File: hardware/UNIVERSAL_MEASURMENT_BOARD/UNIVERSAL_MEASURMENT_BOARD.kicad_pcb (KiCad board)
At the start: 2 copper layers, 9 parts, among them J1 2604-1104, J2 2604-1104, U1 PGA280AIPW, U2 CD4067BM96, U3 CD4067BM96, U4 STM32G0C1KCT6N, U5 ADM3055EBRIZ-RL, U6 ADS8863IDGS, Y2 ECS-1612MV

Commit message: continued
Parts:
- removed the U5 at (148.6, 103.5)
- added C14: 22uF, Capacitor_SMD:C_0805_2012Metric, F.Cu at (137.1, 25.6)
- added C15: 330nF, Capacitor_SMD:C_0805_2012Metric, F.Cu at (137.1, 28.6)
- added C16: 100nF, Capacitor_SMD:C_0805_2012Metric, F.Cu at (137.1, 31.6)
- added C17: 22uF, Capacitor_SMD:C_0805_2012Metric, F.Cu at (137.1, 34.6)
- added C18: 100nF, Capacitor_SMD:C_0603_1608Metric, F.Cu at (154.7, 48.0)
- added C19: 22uF, Capacitor_SMD:C_0805_2012Metric, F.Cu at (137.1, 37.6)
- added C20: 22uF, Capacitor_SMD:C_0805_2012Metric, F.Cu at (137.1, 40.6)
- added C21: 100nF, Capacitor_SMD:C_0603_1608Metric, F.Cu at (154.7, 50.5)
- added C22: 22uF, Capacitor_SMD:C_0805_2012Metric, F.Cu at (137.1, 43.6)
- added C23: 22uF, Capacitor_SMD:C_0805_2012Metric, F.Cu at (137.1, 46.6)
- added C24: 22uF, Capacitor_SMD:C_0805_2012Metric, F.Cu at (137.1, 49.6)
- added C25: 22uF, Capacitor_SMD:C_0805_2012Metric, F.Cu at (141.6, 25.6)
- added C26: 22uF, Capacitor_SMD:C_0805_2012Metric, F.Cu at (141.6, 28.6)
- added C27: 100nF, Capacitor_SMD:C_0805_2012Metric, F.Cu at (141.6, 31.6)
- added C28: 10uF, Capacitor_SMD:C_0805_2012Metric, F.Cu at (141.6, 34.6)
- added C29: 22uF, Capacitor_SMD:C_0805_2012Metric, F.Cu at (141.6, 37.6)
- added C30: 100nF, Capacitor_SMD:C_0603_1608Metric, F.Cu at (154.7, 53.0)
- added C31: 22uF, Capacitor_SMD:C_0805_2012Metric, F.Cu at (141.6, 40.6)
- added C32: 22uF, Capacitor_SMD:C_0805_2012Metric, F.Cu at (141.6, 43.6)
- added C33: 100nF, Capacitor_SMD:C_0603_1608Metric, F.Cu at (154.7, 55.5)
- added C34: 22uF, Capacitor_SMD:C_0805_2012Metric, F.Cu at (141.6, 46.6)
- added C35: 100nF, Capacitor_SMD:C_0805_2012Metric, F.Cu at (141.6, 49.6)
- added C36: 10uF, Capacitor_SMD:C_0805_2012Metric, F.Cu at (146.0, 25.6)
- added C37: 22uF, Capacitor_SMD:C_0805_2012Metric, F.Cu at (146.0, 28.6)
- added C38: 22uF, Capacitor_SMD:C_0805_2012Metric, F.Cu at (146.0, 31.6)
- added C39: 22uF, Capacitor_SMD:C_0805_2012Metric, F.Cu at (146.0, 34.6)
- added C40: 22uF, Capacitor_SMD:C_0805_2012Metric, F.Cu at (146.0, 37.6)
- added C41: 22uF, Capacitor_SMD:C_0805_2012Metric, F.Cu at (146.0, 40.6)
- added C42: 22uF, Capacitor_SMD:C_0805_2012Metric, F.Cu at (146.0, 43.6)
- added C43: 330nF, Capacitor_SMD:C_0805_2012Metric, F.Cu at (146.0, 46.6)
- added C44: 100nF, Capacitor_SMD:C_0805_2012Metric, F.Cu at (146.0, 49.6)
- added C45: 22uF, Capacitor_SMD:C_0805_2012Metric, F.Cu at (150.5, 25.6)
- added C46: 100nF, Capacitor_SMD:C_0603_1608Metric, F.Cu at (154.7, 58.0)
- added C47: 22uF, Capacitor_SMD:C_0805_2012Metric, F.Cu at (150.5, 28.6)
- added C48: 22uF, Capacitor_SMD:C_0805_2012Metric, F.Cu at (150.5, 31.6)
- added C49: 100nF, Capacitor_SMD:C_0603_1608Metric, F.Cu at (154.7, 60.5)
- added C50: 22uF, Capacitor_SMD:C_0805_2012Metric, F.Cu at (150.5, 34.6)
- added C51: 22uF, Capacitor_SMD:C_0805_2012Metric, F.Cu at (150.5, 37.6)
- added C52: 22uF, Capacitor_SMD:C_0805_2012Metric, F.Cu at (150.5, 40.6)
- added C53: 100nF, Capacitor_SMD:C_0805_2012Metric, F.Cu at (150.5, 43.6)
- added C55: 100nF, Capacitor_SMD:C_0805_2012Metric, F.Cu at (150.5, 46.6)
- added C57: -F, Capacitor_SMD:C_0805_2012Metric, F.Cu at (150.5, 49.6)
- added J10: 2604-1104, 2604-1104:26041104, F.Cu at (58.2, 74.8)
- added J11: 2604-1104, 2604-1104:26041104, F.Cu at (58.2, 97.6)
- added J12: 2604-1104, 2604-1104:26041104, F.Cu at (58.2, 120.5)
- added J13: 2604-1104, 2604-1104:26041104, F.Cu at (58.2, 143.3)
- added J14: 2604-1104, 2604-1104:26041104, F.Cu at (58.2, 166.2)
- added J15: 2604-1104, 2604-1104:26041104, F.Cu at (83.7, 29.1)
- added J16: PRG, Connector_PinHeader_1.00mm:PinHeader_1x05_P1.00mm_Vertical, F.Cu at (131.2, 25.6)
- added J17: 2604-1104, 2604-1104:26041104, F.Cu at (83.7, 51.9)
- added J18: 2604-1104, 2604-1104:26041104, F.Cu at (83.7, 74.8)
- added J19: 2604-1104, 2604-1104:26041104, F.Cu at (83.7, 97.6)
- added J20: 2604-1104, 2604-1104:26041104, F.Cu at (83.7, 120.5)
- added J21: 2604-1104, 2604-1104:26041104, F.Cu at (83.7, 143.3)
- added J22: 2604-1104, 2604-1104:26041104, F.Cu at (83.7, 166.2)
- added J23: 2604-1104, 2604-1104:26041104, F.Cu at (109.2, 29.1)
- added J24: 2604-1104, 2604-1104:26041104, F.Cu at (109.2, 51.9)
- added J25: 2604-1104, 2604-1104:26041104, F.Cu at (109.2, 74.8)
- added J26: 2604-1104, 2604-1104:26041104, F.Cu at (109.2, 97.6)
- added J27: 2604-1104, 2604-1104:26041104, F.Cu at (109.2, 120.5)
- added J3: 2604-1104, 2604-1104:26041104, F.Cu at (32.7, 74.8)
- added J4: 2604-1104, 2604-1104:26041104, F.Cu at (32.7, 97.6)
- added J5: 2604-1104, 2604-1104:26041104, F.Cu at (32.7, 120.5)
- added J6: 2604-1104, 2604-1104:26041104, F.Cu at (32.7, 143.3)
- added J7: 2604-1104, 2604-1104:26041104, F.Cu at (32.7, 166.2)
- added J8: 2604-1104, 2604-1104:26041104, F.Cu at (58.2, 29.1)
- added J9: 2604-1104, 2604-1104:26041104, F.Cu at (58.2, 51.9)
- added L1: 68uH/1.4A, Inductor_SMD:L_TDK_VLS6045EX_VLS6045AF, F.Cu at (156.5, 27.8)
- added L2: 68uH/1.4A, Inductor_SMD:L_TDK_VLS6045EX_VLS6045AF, F.Cu at (156.5, 35.4)
- added L3: 68uH/1.4A, Inductor_SMD:L_TDK_VLS6045EX_VLS6045AF, F.Cu at (156.5, 42.9)
- added U10: TPS54202HDDCR, TPS54202HDDCR:SOT95P280X110-6N, F.Cu at (159.3, 53.6)
- added U12: TPS54202HDDCR, TPS54202HDDCR:SOT95P280X110-6N, F.Cu at (159.3, 58.2)
- added U13: ICL7662EBA+, ICL7662EBA+:SOIC127P600X175-8N, F.Cu at (139.1, 54.4)
- added U14: ADM3055EBRIZ-RL, ADM3055EBRIZ-RL:SOIC127P1030X264-20N, F.Cu at (141.3, 72.3)
- added U7: TPS54202HDDCR, TPS54202HDDCR:SOT95P280X110-6N, F.Cu at (159.3, 49.0)
- added U8: AMS1117-3.3, Package_TO_SOT_SMD:SOT-223-3_TabPin2, F.Cu at (165.3, 28.2)
- added U9: AMS1117-3.3, Package_TO_SOT_SMD:SOT-223-3_TabPin2, F.Cu at (165.3, 36.6)
- moved J1 155.8 mm to (32.7, 29.1)
- moved J2 155.8 mm to (32.7, 51.9)
- moved U1 30.5 mm to (188.8, 120.6)
- moved U2 30.5 mm to (190.8, 112.5)
- moved U3 30.5 mm to (148.9, 115.3)
- moved U4 30.5 mm to (146.8, 128.7)
- moved U5 30.5 mm to (161.8, 115.3)
- moved Y1 30.5 mm to (194.8, 120.5)
- renumbered U6 to U1, U4 to U2, U2 to U3, U1 to U4, U3 to U5, Y2 to Y1
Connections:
- net +15V renamed +15VA
- net +3.3V renamed +3.3VA
- net -15V renamed -15VA
- J1 pad 5: Net-(J1-3.1) -> /connectors/A1P
- J1 pad 6: Net-(J1-3.1) -> /connectors/A1P
- J1 pad 7: Net-(J1-4.1) -> /connectors/A1N
- J1 pad 8: Net-(J1-4.1) -> /connectors/A1N
- J2 pad 1: Net-(J2-1.1) -> /connectors/A6N
- J2 pad 2: Net-(J2-1.1) -> /connectors/A6N
- J2 pad 3: Net-(J2-2.1) -> GND
- J2 pad 4: Net-(J2-2.1) -> GND
- U1 pad 2: +3V3 -> +3V3A
- U3 pad 16: /mux & pga/A16P -> /connectors/A16P
- U3 pad 17: /mux & pga/A15P -> /connectors/A15P
- U3 pad 18: /mux & pga/A14P -> /connectors/A14P
- U3 pad 19: /mux & pga/A13P -> /connectors/A13P
- U3 pad 2: /mux & pga/A8P -> /connectors/A8P
- U3 pad 20: /mux & pga/A12P -> /connectors/A12P
- U3 pad 21: /mux & pga/A11P -> /connectors/A11P
- U3 pad 22: /mux & pga/A10P -> /connectors/A10P
- U3 pad 23: /mux & pga/A9P -> /connectors/A9P
- U3 pad 3: /mux & pga/A7P -> /connectors/A7P
- U3 pad 4: /mux & pga/A6P -> /connectors/A6P
- U3 pad 5: /mux & pga/A5P -> /connectors/A5P
- U3 pad 6: /mux & pga/A4P -> /connectors/A4P
- U3 pad 7: /mux & pga/A3P -> /connectors/A3P
- U3 pad 8: /mux & pga/A2P -> /connectors/A2P
- U3 pad 9: /mux & pga/A1P -> /connectors/A1P
- U5 pad 16: /mux & pga/A16N -> /connectors/A16N
- U5 pad 17: /mux & pga/A15N -> /connectors/A15N
- U5 pad 18: /mux & pga/A14N -> /connectors/A14N
- U5 pad 19: /mux & pga/A13N -> /connectors/A13N
- U5 pad 2: /mux & pga/A8N -> /connectors/A8N
- U5 pad 20: /mux & pga/A12N -> /connectors/A12N
- U5 pad 21: /mux & pga/A11N -> /connectors/A11N
- U5 pad 22: /mux & pga/A10N -> /connectors/A10N
- U5 pad 23: /mux & pga/A9N -> /connectors/A9N
- U5 pad 3: /mux & pga/A7N -> /connectors/A7N
- U5 pad 4: /mux & pga/A6N -> /connectors/A6N
- U5 pad 5: /mux & pga/A5N -> /connectors/A5N
- U5 pad 6: /mux & pga/A4N -> /connectors/A4N
- U5 pad 7: /mux & pga/A3N -> /connectors/A3N
- U5 pad 8: /mux & pga/A2N -> /connectors/A2N
- U5 pad 9: /mux & pga/A1N -> /connectors/A1N

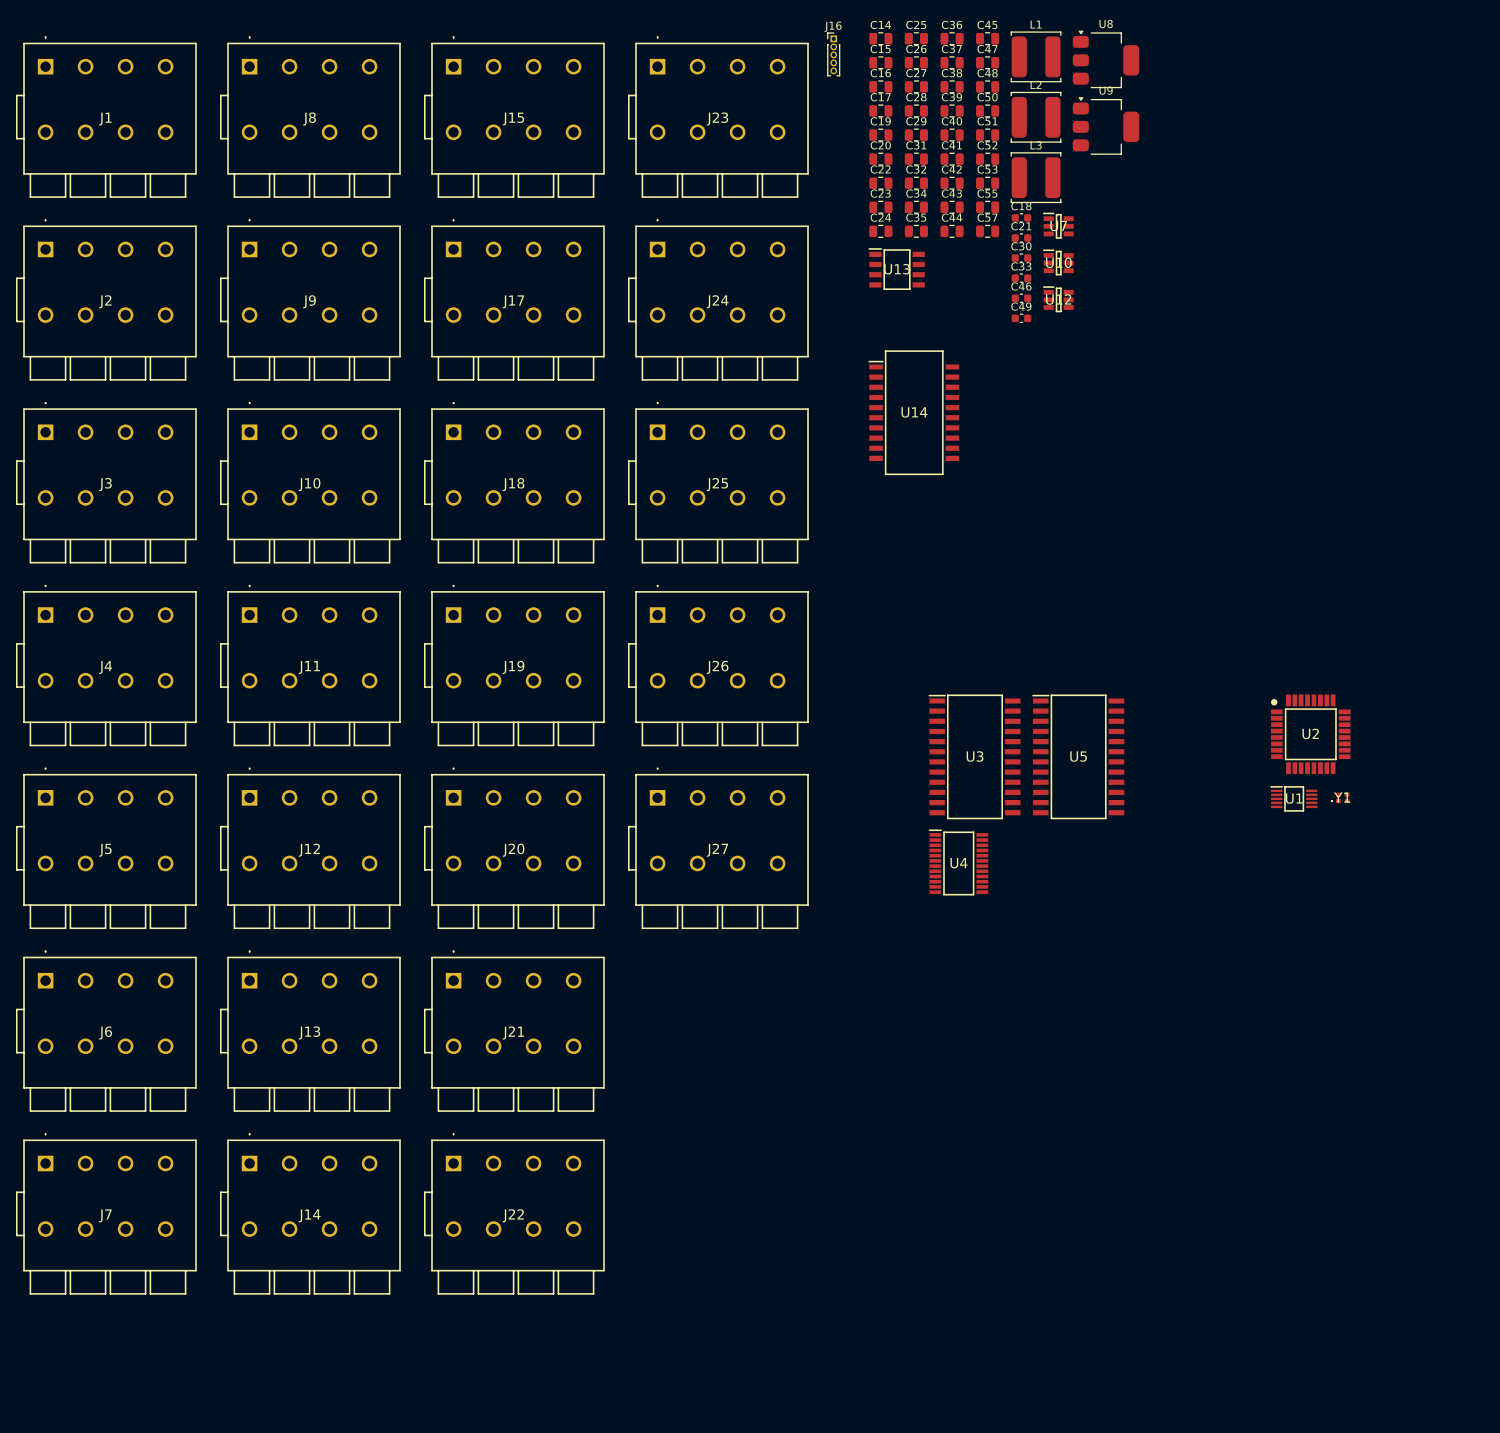
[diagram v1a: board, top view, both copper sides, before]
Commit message: schematic review corrections
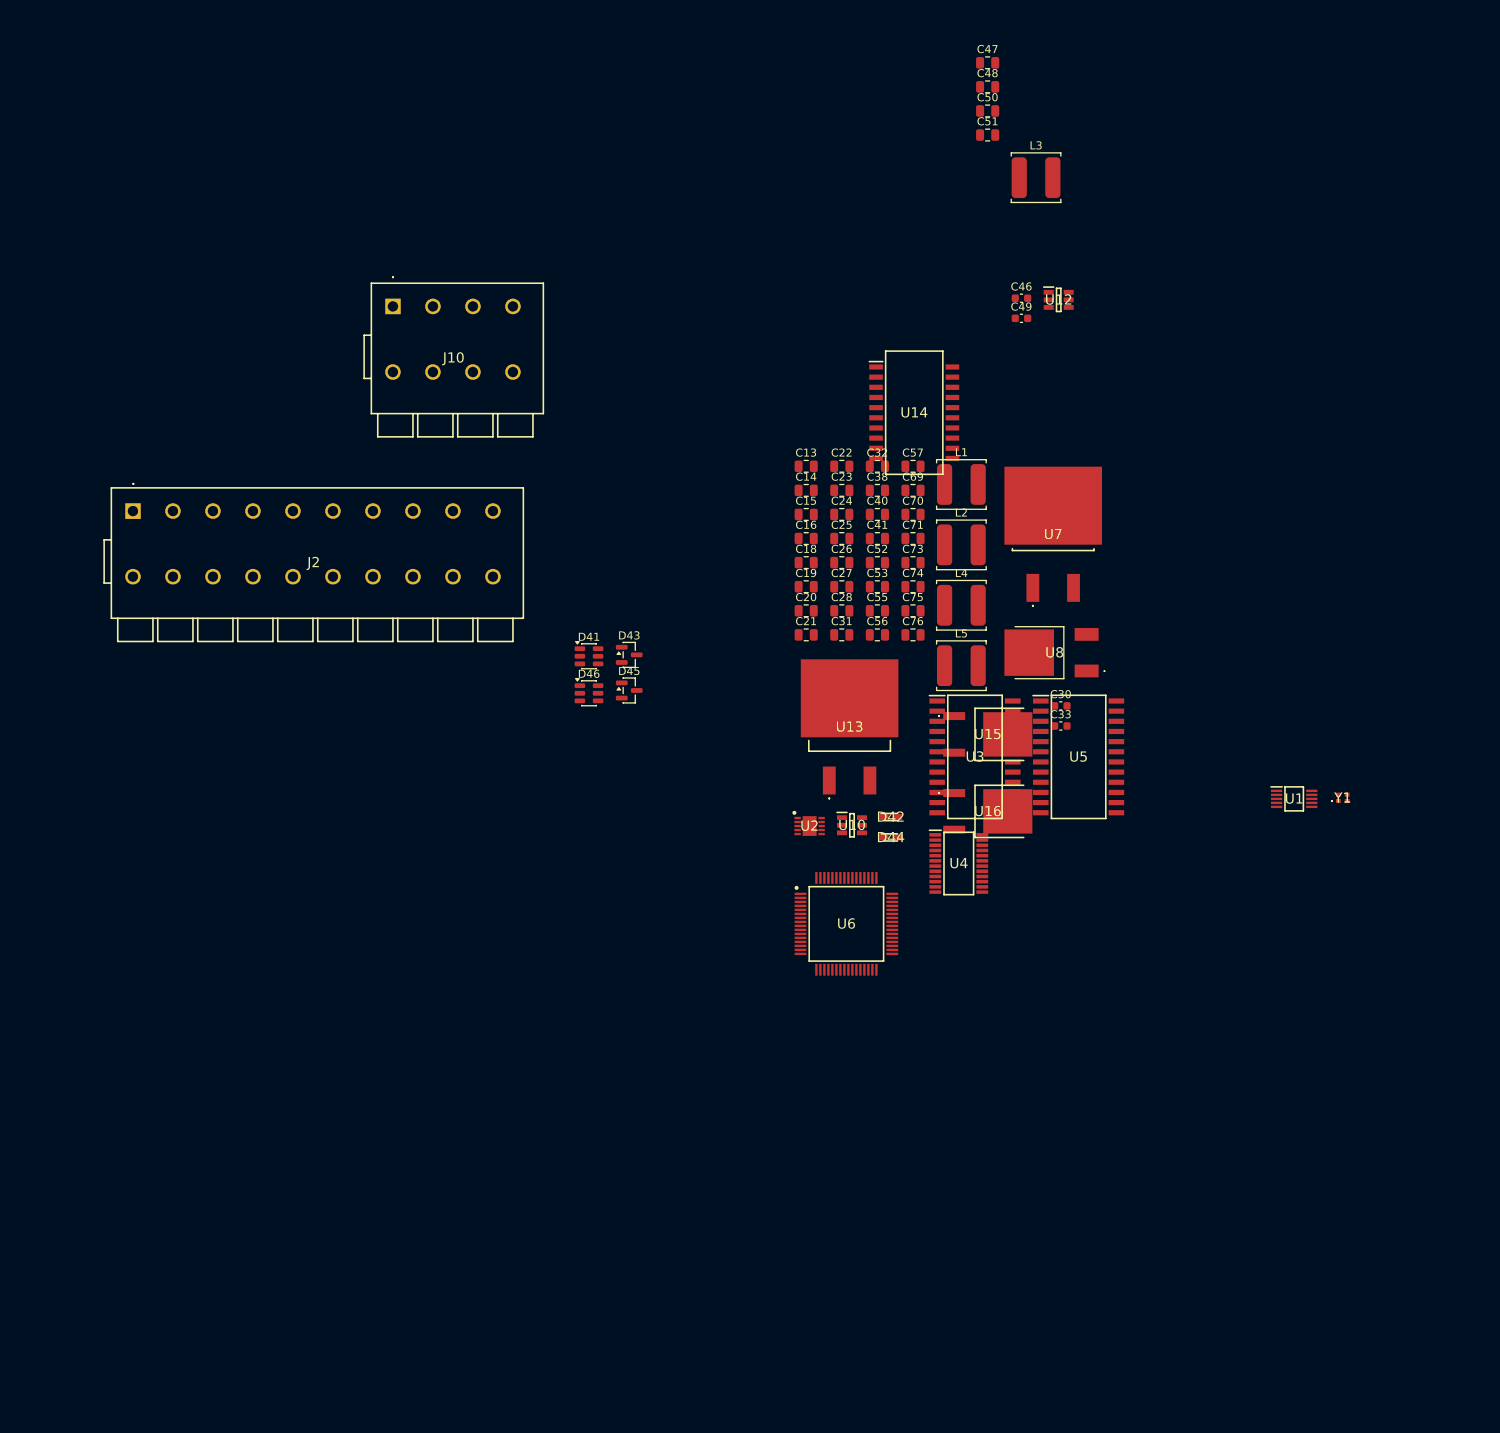
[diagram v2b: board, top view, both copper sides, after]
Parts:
- removed C17, C29, C34, C37, C39, C42, C45: 22uF, Capacitor_SMD:C_0805_2012Metric
- removed C35, C44: 100nF, Capacitor_SMD:C_0805_2012Metric
- removed C36: 10uF, Capacitor_SMD:C_0805_2012Metric
- removed C43: 330nF, Capacitor_SMD:C_0805_2012Metric
- removed J1, J11, J12, J13, J14, J15, J17, J18, J19, J20, J21, J22, J23, J24, J25, J26, J27, J3, J4, J5, J6, J7, J8, J9: 2604-1104, 2604-1104:26041104
- removed J16: PRG, Connector_PinHeader_1.00mm:PinHeader_1x05_P1.00mm_Vertical
- removed U9: AMS1117-3.3, Package_TO_SOT_SMD:SOT-223-3_TabPin2
- added C13: 100nF, Capacitor_SMD:C_0805_2012Metric, F.Cu at (127.8, 79.0)
- added C56: 330nF, Capacitor_SMD:C_0805_2012Metric, F.Cu at (136.7, 100.1)
- added C69: 22uF, Capacitor_SMD:C_0805_2012Metric, F.Cu at (141.1, 82.0)
- added C70: 330nF, Capacitor_SMD:C_0805_2012Metric, F.Cu at (141.1, 85.0)
- added C71: 100nF, Capacitor_SMD:C_0805_2012Metric, F.Cu at (141.1, 88.0)
- added C73: 22uF, Capacitor_SMD:C_0805_2012Metric, F.Cu at (141.1, 91.0)
- added C74: 330nF, Capacitor_SMD:C_0805_2012Metric, F.Cu at (141.1, 94.1)
- added C75: 100nF, Capacitor_SMD:C_0805_2012Metric, F.Cu at (141.1, 97.1)
- added C76: 22uF, Capacitor_SMD:C_0805_2012Metric, F.Cu at (141.1, 100.1)
- added D41: 3.6V/400W, Package_TO_SOT_SMD:SOT-23-6, F.Cu at (100.6, 102.8)
- added D42: CDBU0340, CDBU0340:DIOM179X85N, F.Cu at (138.3, 122.8)
- added D43: BZX84C5V6, Package_TO_SOT_SMD:SOT-23, F.Cu at (105.7, 102.6)
- added D44: CDBU0340, CDBU0340:DIOM179X85N, F.Cu at (138.3, 125.4)
- added D45: BZX84C3V6-E3-08, Package_TO_SOT_SMD:SOT-23, F.Cu at (105.7, 107.0)
- added D46: 3.6V/400W, Package_TO_SOT_SMD:SOT-23-6, F.Cu at (100.6, 107.4)
- added L4: 10uH, Inductor_SMD:L_TDK_VLS6045EX_VLS6045AF, F.Cu at (147.2, 96.4)
- added L5: 15uH, Inductor_SMD:L_TDK_VLS6045EX_VLS6045AF, F.Cu at (147.2, 103.9)
- added U15: TLV76133KVUR, TLV76133KVUR:TLV76133KVUR, F.Cu at (150.6, 112.5)
- added U16: TLV76133KVUR, TLV76133KVUR:TLV76133KVUR, F.Cu at (150.6, 122.1)
- added U6: STM32G484RET3, STM32G484RET3:QFP50P1200X1200X160-64N, F.Cu at (132.8, 136.2)
- C16: value 100nF -> 220nF
- C18: value 100nF -> 10uF; footprint Capacitor_SMD:C_0603_1608Metric -> Capacitor_SMD:C_0805_2012Metric
- C19, C20, C23: value 22uF -> 1uF
- C21: value 100nF -> 4.7uF; footprint Capacitor_SMD:C_0603_1608Metric -> Capacitor_SMD:C_0805_2012Metric
- C22: value 22uF -> 100nF
- C24: value 22uF -> 10uF
- C25: value 22uF -> 75pF
- C27: value 100nF -> 330nF
- C28: value 10uF -> 220nF
- C52: value 22uF -> 330nF
- C55: value 100nF -> 22uF
- C57: value -F -> 100nF
- J2: value 2604-1104 -> 2606-1110_010-000; footprint 2604-1104:26041104 -> 2604-1110:26041110
- L1: value 68uH/1.4A -> 2.2uH
- U13: value ICL7662EBA+ -> L7805ABD2T-TR; footprint ICL7662EBA+:SOIC127P600X175-8N -> L7805ABD2T-TR:L7805ABD2TTR
- U2: value STM32G0C1KCT6N -> LT3471EDD#PBF; footprint STM32G0C1KCT6N:QFP80P900X900X160-32N -> LT3471EDD#PBF:SON50P300X300X80-11N-D
- U7: value TPS54202HDDCR -> L7812ABD2T-TR; footprint TPS54202HDDCR:SOT95P280X110-6N -> L7812ABD2T-TR:L7812ABD2TTR
- U8: value AMS1117-3.3 -> MC7815BDTRKG; footprint Package_TO_SOT_SMD:SOT-223-3_TabPin2 -> MC7815BDTRKG:NVD5117PLT4GVF01
- moved U8 74.9 mm to (153.9, 102.3)
- moved U10 74.9 mm to (133.5, 123.9)
- moved U2 63.7 mm to (128.2, 124.0)
- moved C26 63.2 mm to (132.2, 91.0)
- moved C27 63.2 mm to (132.2, 94.1)
- moved C25 63.2 mm to (132.2, 88.0)
- moved C28 63.2 mm to (132.2, 97.1)
- moved C31 60.2 mm to (132.2, 100.1)
- moved U13 57.8 mm to (133.2, 111.9)
- moved C15 57.2 mm to (127.8, 85.0)
- moved C19 57.2 mm to (127.8, 94.1)
- moved C14 57.2 mm to (127.8, 82.0)
- moved C20 57.2 mm to (127.8, 97.1)
- moved C16 57.2 mm to (127.8, 88.0)
- moved C21 56.4 mm to (127.8, 100.1)
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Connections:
- net +24V renamed Net-(U12-VIN)
- C18 pad 1: Net-(U7-BOOT) -> GND
- C18 pad 2: Net-(U7-SW) -> +15VF
- C19 pad 2: +18V -> Net-(U2-~{SHDN}/SS1)
- C20 pad 2: +18V -> Net-(U2-~{SHDN}/SS2)
- C22 pad 1: +12V -> GND
- C22 pad 2: GND -> Net-(U2-FB1P)
- C23 pad 1: +12V -> Net-(D44-A)
- C23 pad 2: GND -> Net-(U2-SW2)
- C24 pad 1: +12V -> GND
- C24 pad 2: GND -> -18V
- C25 pad 1: +12V -> -18V
- C25 pad 2: GND -> Net-(U2-FB2P)
- C26 pad 1: +5V -> GND
- C26 pad 2: GND -> -18V
- C27 pad 1: +5V -> GND
- C27 pad 2: GND -> -18V
- C28 pad 1: +3.3V -> GND
- C28 pad 2: GND -> -15VA
- C31 pad 2: +18V -> Net-(U10-VIN)
- C32 pad 2: +18V -> Net-(U10-VIN)
- C33 pad 2: +18V -> Net-(U10-VIN)
- C38 pad 1: +5V -> +7V
- C40 pad 1: +5V -> +15V
- C41 pad 1: +5V -> +7V
- C50 pad 1: +18V -> +15V
- C51 pad 1: +18V -> +15V
- C52 pad 1: +18V -> +15V
- C53 pad 1: +18V -> +12VA
- C55 pad 1: -18V -> +7V
- C57 pad 1: Net-(U13-OSC) -> +5VA
- J10 pad 3: /can/CANH -> GND
- J10 pad 4: /can/CANH -> GND
- J10 pad 5: /can/CANL -> /can/CANH
- J10 pad 6: /can/CANL -> /can/CANH
- J10 pad 7: GND -> /can/CANL
- J10 pad 8: GND -> /can/CANL
- J2 pad 1: /connectors/A6N -> Net-(F14-Pad2)
- J2 pad 2: /connectors/A6N -> Net-(F17-Pad2)
- J2 pad 3: GND -> /connectors/A3P
- J2 pad 4: GND -> /connectors/A3N
- J2 pad 5: Net-(J2C-3) -> GND
- J2 pad 6: Net-(J2C-3) -> Net-(F20-Pad2)
- J2 pad 7: Net-(J2D-4) -> Net-(F23-Pad2)
- J2 pad 8: Net-(J2D-4) -> /connectors/A4P
- L1 pad 1: Net-(U7-SW) -> +15VF
- L1 pad 2: +12V -> Net-(D42-A)
- L2 pad 2: +5V -> +7V
- L3 pad 2: +18V -> +15V
- U10 pad 3: +18V -> Net-(U10-VIN)
- U13 pad 1: unconnected-(U13-TEST-Pad1) -> +7V
- U13 pad 2: Net-(U13-CAP+) -> GND
- U13 pad 3: GND -> +5VA
- U2 pad 1: unconnected-(U2-PB9-Pad1) -> Net-(U2-FB1N)
- U2 pad 10: unconnected-(U2-PA3-Pad10) -> Net-(D42-A)
- U2 pad 11: unconnected-(U2-PA4-Pad11) -> GND
- U2 pad 2: /mcu & adc/OSC -> Net-(U2-FB1P)
- U2 pad 3: unconnected-(U2-PC15-OSC32_OUT-Pad3) -> Net-(U2-FB1P)
- U2 pad 4: +3V3 -> Net-(U2-FB2P)
- U2 pad 6: unconnected-(U2-PF2-NRST-Pad6) -> Net-(U2-SW2)
- U2 pad 7: unconnected-(U2-PA0-Pad7) -> Net-(U2-~{SHDN}/SS2)
- U2 pad 8: unconnected-(U2-PA1-Pad8) -> +15VF
- U2 pad 9: unconnected-(U2-PA2-Pad9) -> Net-(U2-~{SHDN}/SS1)
- U3 pad 12: -15VA -> GND
- U3 pad 16: /connectors/A16P -> /mux & pga/A16P
- U3 pad 17: /connectors/A15P -> /mux & pga/A15P
- U3 pad 18: /connectors/A14P -> /mux & pga/A14P
- U3 pad 19: /connectors/A13P -> /mux & pga/A13P
- U3 pad 20: /connectors/A12P -> /mux & pga/A12P
- U3 pad 21: /connectors/A11P -> /mux & pga/A11P
- U3 pad 22: /connectors/A10P -> /mux & pga/A10P
- U3 pad 23: /connectors/A9P -> /mux & pga/A9P
- U5 pad 12: -15VA -> GND
- U5 pad 16: /connectors/A16N -> /mux & pga/A16N
- U5 pad 17: /connectors/A15N -> /mux & pga/A15N
- U5 pad 18: /connectors/A14N -> /mux & pga/A14N
- U5 pad 19: /connectors/A13N -> /mux & pga/A13N
- U5 pad 20: /connectors/A12N -> /mux & pga/A12N
- U5 pad 21: /connectors/A11N -> /mux & pga/A11N
- U5 pad 22: /connectors/A10N -> /mux & pga/A10N
- U5 pad 23: /connectors/A9N -> /mux & pga/A9N
- U7 pad 1: GND -> +15V
- U7 pad 2: Net-(U7-SW) -> GND
- U7 pad 3: +18V -> +12VA
- U8 pad 1: GND -> +18V
- U8 pad 2: +3.3V -> GND
- U8 pad 3: +5V -> +15VA
- Y1 pad 3: /mcu & adc/OSC -> /mcu & adc/HSE
